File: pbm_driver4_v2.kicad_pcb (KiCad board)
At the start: 4 copper layers, 30 x 70 mm, 96 parts, among them J1 Conn_02x10_Odd_Even, J2 Conn_01x10, J3 Conn_01x02, J4 Conn_01x02, Q1 PSMN4R0-30YLDX, Q2 PSMN4R0-30YLDX, Q3 PSMN4R0-30YLDX, Q4 PSMN4R0-30YLDX, U1 ADA4099-2xR, U11 TS5A3159ADCK, U12 TS5A3159ADCK, U13 TS5A3159ADCK, U14 TS5A3159ADCK, U2 ADA4099-2xR, U21 OPA365AIDBV, U22 OPA365AIDBV, U23 OPA365AIDBV, U24 OPA365AIDBV, U3 ADA4099-1, U4 ADA4099-1, U5 ADA4099-1, U6 ADA4099-1

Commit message: Commit WIP begore migration to KiCad V10.
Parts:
- moved R21 4.50 mm to (4.50, -19.4)
- moved C61 4.40 mm to (2.20, -22.0)
- moved R61 4.40 mm to (4.50, -22.0)
- moved R71 4.40 mm to (6.80, -22.0)
- moved C21 4.00 mm to (5.70, -25.4)
- moved R51 4.00 mm to (2.20, -25.4)
- moved U21 4.00 mm to (5.70, -25.4)
- moved C41 3.60 mm to (4.50, -28.8)
- moved C51 3.60 mm to (6.80, -28.8)
- moved R41 3.60 mm to (2.20, -28.8)
- moved C11 3.10 mm to (4.50, -32.0)
- moved C12 3.10 mm to (11.5, -32.0)
- moved U11 3.10 mm to (4.50, -32.0)
- moved U12 3.10 mm to (11.5, -32.0)
- moved U13 3.10 mm to (18.5, -32.0)
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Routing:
- net /Driver1/SENSE_R: track 38.6 -> 15.3 mm
- net /SENSE1: track 16.7 -> 5.63 mm
- net /SEL1: track 28.9 -> 17.9 mm
- net GND: track 34.9 -> 26.8 mm, vias 18 -> 13
- net /Driver1/FILTER_FB: track 7.46 -> 0.00 mm
- net /Driver1/FILTER: track 5.42 -> 0.00 mm
- net /DAC1: track 8.95 -> 6.16 mm
- net +3.3V: track 3.28 -> 1.05 mm, vias 3 -> 2
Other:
- board text added: "LED Array is 58.5 mm wide and 30.5 mm deep"
- board text added: "LED Bezzel is 80 mm wide x 47 mm deep"
- board text added: "Mtg hole grid is 68.58 mm (2.7{dblquote}) wide and 35.56 (1.4{dblquote}) mm deep"

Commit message: Migrate to KiCad 10.
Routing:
- net GND: vias 13 -> 14
- net +3.3V: vias 2 -> 1

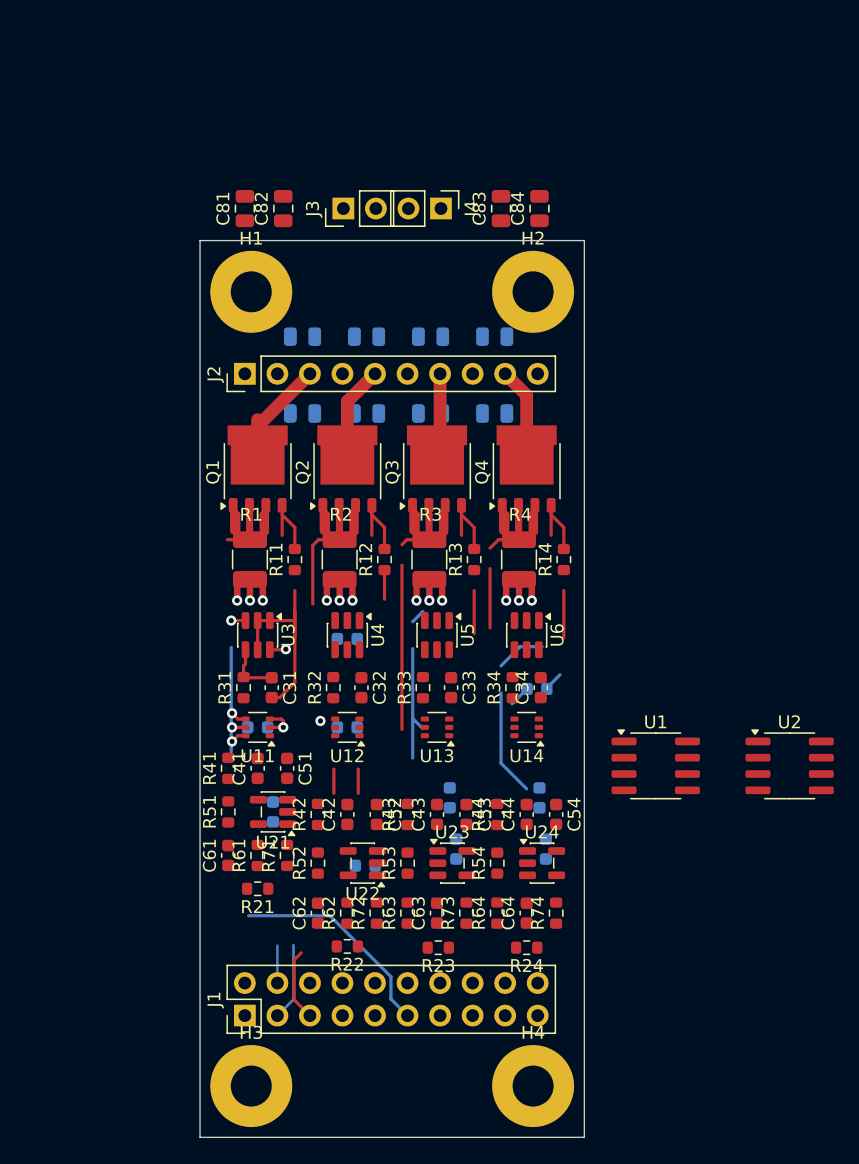
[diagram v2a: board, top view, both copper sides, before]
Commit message: Initial placement on 45 x 30 mm outline. Dropped sense apms. Switch to two 2x6 connectors.
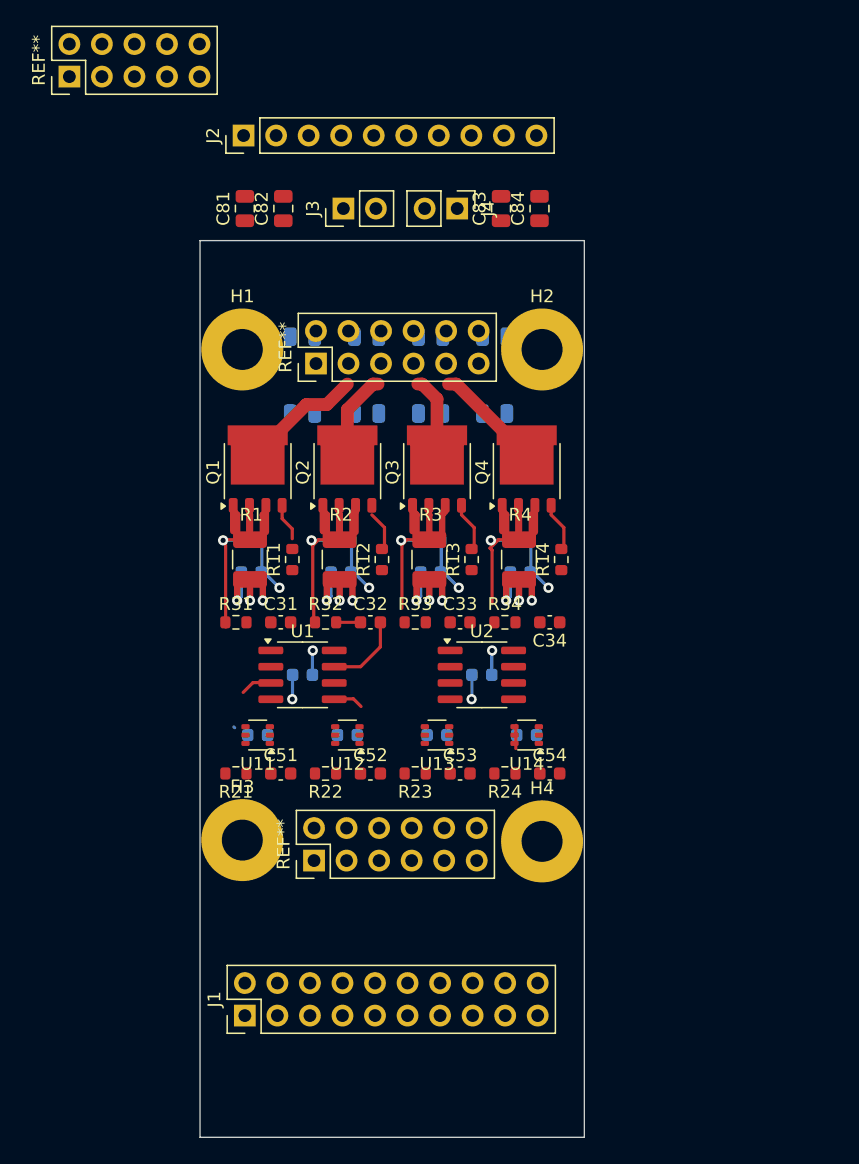
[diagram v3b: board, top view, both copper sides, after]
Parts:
- removed C21, C22, C23, C24, C61, C62, C63, C64: 100nF 50V, $Local:C_0603_1608Metric
- removed R51, R52, R53, R54, R71, R72, R73, R74: 10K 1%, $Local:R_0603_1608Metric
- removed R61, R62, R63, R64: 90.9K 1%, $Local:R_0603_1608Metric
- removed U21, U22, U23, U24: OPA365AIDBV, $Local:SOT-23-5
- removed U3, U4, U5, U6: ADA4099-1, $Local:TSOT-23-6
- added REF**: PinHeader_2x06_P2.54mm_Vertical, $Local:PinHeader_2x06_P2.54mm_Vertical, F.Cu at (9.05, -60.4)
- added REF**: PinHeader_2x05_P2.54mm_Vertical, $Local:PinHeader_2x05_P2.54mm_Vertical, F.Cu at (-10.2, -82.8)
- added REF**: PinHeader_2x06_P2.54mm_Vertical, $Local:PinHeader_2x06_P2.54mm_Vertical, F.Cu at (8.90, -21.6)
- C41, C42, C43, C44, R41, R42, R43, R44: moved to B.Cu
- moved U1 28.5 mm to (8.00, -36.1)
- moved U2 25.1 mm to (22.0, -36.1)
- moved R42 21.5 mm to (11.0, -46.6), turned to 180 degrees
- moved R43 21.5 mm to (18.0, -46.6), turned to 180 degrees
- moved R44 21.5 mm to (25.0, -46.6), turned to 180 degrees
- moved H3 19.2 mm to (3.30, -23.2)
- moved H4 19.1 mm to (26.7, -23.1)
- moved C42 18.9 mm to (11.0, -44.1), turned to 180 degrees
- moved C43 18.9 mm to (18.0, -44.1), turned to 180 degrees
- moved C44 18.9 mm to (25.0, -44.1), turned to 180 degrees
- moved J2 18.6 mm to (3.40, -78.2)
- moved R41 17.9 mm to (4.00, -46.6), turned to 180 degrees
- moved C41 15.3 mm to (4.00, -44.1), turned to 180 degrees
- moved R23 13.7 mm to (16.8, -28.4)
- moved R24 13.7 mm to (23.8, -28.4)
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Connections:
- C41 pad 1: /Driver1/FILTER -> /SENSE1
- C42 pad 1: /Driver2/FILTER -> /SENSE2
- C43 pad 1: /Driver3/FILTER -> /SENSE3
- C44 pad 1: /Driver4/FILTER -> /SENSE4
- R41 pad 1: /Driver1/FILTER -> /SENSE1
- R42 pad 1: /Driver2/FILTER -> /SENSE2
- R43 pad 1: /Driver3/FILTER -> /SENSE3
- R44 pad 1: /Driver4/FILTER -> /SENSE4
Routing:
- net /SEL1: track 17.9 -> 0.00 mm, vias 1 -> 0
- net /Driver1/OUT: track 14.1 -> 0.00 mm
- net /Driver3/REF: track 10.8 -> 0.00 mm
- net /Driver4/REF: track 12.1 -> 2.02 mm
- net /Driver3/SENSE_R: track 28.6 -> 18.9 mm, vias 0 -> 1
- net /Driver1/REF: track 10.7 -> 2.47 mm, vias 2 -> 0
- net /Driver1/SENSE_R: track 15.3 -> 23.0 mm, vias 0 -> 1
- net GND: track 26.8 -> 34.3 mm
- net /DAC1: track 6.16 -> 0.00 mm
- net /DAC2: track 4.82 -> 0.00 mm
- net /SENSE4: track 0.00 -> 4.48 mm, vias 0 -> 1
- net /SENSE3: track 0.00 -> 4.44 mm, vias 0 -> 1
- net /SENSE2: track 0.00 -> 4.44 mm, vias 0 -> 1
- net /Driver1/FB: track 4.39 -> 0.00 mm
- net /Driver2/OUT: track 2.27 -> 6.16 mm
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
